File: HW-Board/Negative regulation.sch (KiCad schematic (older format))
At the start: 26 parts, among them Q3 BCX56, U10 AD5245, U11 OP07, U12 OP07, U13 OP07, U14 INA219POS, U15 OP07, U9 MCP4725

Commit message: sync
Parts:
- added Rin1: 100K 1%, symbol Device:R
- renumbered Rin1 to Rf1, Rf1 to Rf2, R11 to Rf3, R10 to Rin3
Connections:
- net at Rf1.1, U11.2 (-): now also Rin1.2; no longer U10.7 (B)
- new net: Rin1.1, U10.7 (B)
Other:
- note added: "Flip to negative"
- note added: "Flip to positive"
- note added: "LM395?"
- note removed: "Todo:\n\nMerge to fewer opamps"
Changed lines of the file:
@@
 	8050 2900 8000 2900
 $Comp
-L Device:R R10
+L Device:R Rin3
 U 1 1 5D005FD1
 P 8250 2650
-F 0 "R10" V 8043 2650 50  0000 C CNN
+F 0 "Rin3" V 8043 2650 50  0000 C CNN
 F 1 "100K 1%" V 8134 2650 50  0000 C CNN
 F 2 "" V 8180 2650 50  0001 C CNN
@@
 	8250 2950 8250 2850
 $Comp
-L Device:R R11
+L Device:R Rf3
 U 1 1 5D005FD8
 P 8800 3150
-F 0 "R11" V 8593 3150 50  0000 C CNN
+F 0 "Rf3" V 8593 3150 50  0000 C CNN
 F 1 "100K 1%" V 8684 3150 50  0000 C CNN
 F 2 "" V 8730 3150 50  0001 C CNN
@@
 	6950 3000 6950 2900
 $Comp
-L Device:R Rf1
+L Device:R Rf2
 U 1 1 5D006004
 P 7500 3200
-F 0 "Rf1" V 7293 3200 50  0000 C CNN
+F 0 "Rf2" V 7293 3200 50  0000 C CNN
 F 1 "100K 1%" V 7384 3200 50  0000 C CNN
 F 2 "" V 7430 3200 50  0001 C CNN
@@
 Connection ~ 8250 2200
 Connection ~ 6950 2200
-Text Notes 5750 3800 0    50   ~ 0
+Text Notes 3450 950  0    50   ~ 0
 Inverting AMP:\nVout=  -Rf/Rin x Vin
 $Comp
@@
 $EndComp
 $Comp
-L Device:R Rin1
+L Device:R Rf1
 U 1 1 5CFD1CAF
 P 4050 3850
-F 0 "Rin1" V 3843 3850 50  0000 C CNN
+F 0 "Rf1" V 3843 3850 50  0000 C CNN
 F 1 "100K 1%" V 3934 3850 50  0000 C CNN
 F 2 "" V 3980 3850 50  0001 C CNN
@@
 $EndComp
 Wire Wire Line
-	3250 3300 3750 3300
+	3250 3300 3350 3300
 $Comp
 L power:GNDA #PWR0210
@@
 Wire Wire Line
 	3400 3550 3500 3550
-Text Notes 3000 5650 0    50   ~ 0
-Todo:\n\nMerge to fewer opamps
+Text Notes 3900 4200 0    50   ~ 0
+Flip to negative
+$Comp
+L Device:R Rin1
+U 1 1 5CF6E0E8
+P 3500 3300
+F 0 "Rin1" V 3293 3300 50  0000 C CNN
+F 1 "100K 1%" V 3384 3300 50  0000 C CNN
+F 2 "" V 3430 3300 50  0001 C CNN
+F 3 "~" H 3500 3300 50  0001 C CNN
+	1    3500 3300
+	0    -1   -1   0
+$EndComp
+Wire Wire Line
+	3650 3300 3750 3300
+Text Notes 6450 3950 0    50   ~ 0
+Flip to positive
+Wire Notes Line
+	6300 2450 6300 4000
+Wire Notes Line
+	6300 4000 8900 4000
+Wire Notes Line
+	8900 4000 8900 2450
+Wire Notes Line
+	8900 2450 6300 2450
+Wire Notes Line
+	3400 4450 4500 4450
+Wire Notes Line
+	4500 4450 4500 1950
+Wire Notes Line
+	4500 1950 3400 1950
+Wire Notes Line
+	3400 1950 3400 4450
+Text Notes 5800 1850 0    50   ~ 0
+LM395?
 $EndSCHEMATC

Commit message: sync
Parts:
- added C?: 10u, symbol Device:C_Small
- added C?: 100n, symbol Device:C_Small
- added JP?: Jumper, symbol Device:Jumper
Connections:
- net +3V3: now also C?.1, C?.1
- net GNDA: now also C?.2, C?.2
- net at Rin1.1: now also U10.1 (W), JP?.2; no longer U10.7 (B)
- net at U9.1 (VoutA): now also U10.7 (B), JP?.1; no longer U10.1 (W)
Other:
- moved on the sheet: C26, C27, Rin1, U10, U9

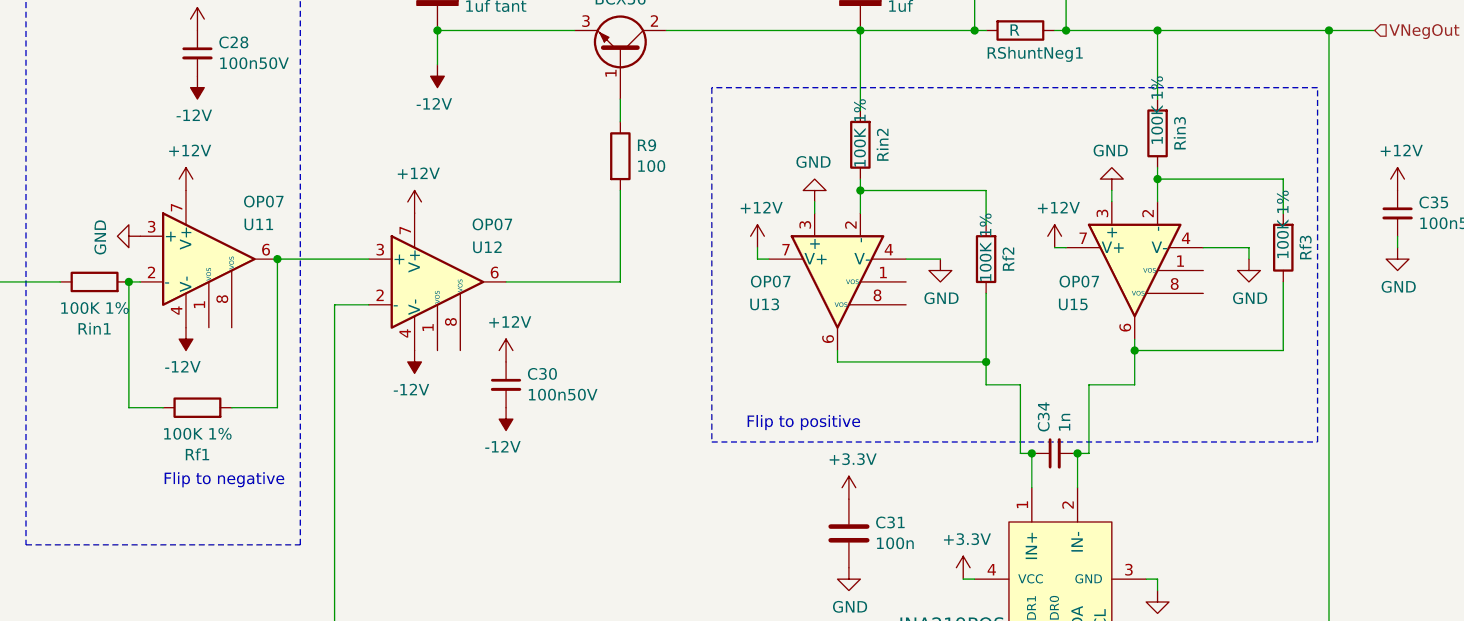
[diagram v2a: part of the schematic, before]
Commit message: Changed OPAMP on negative rail
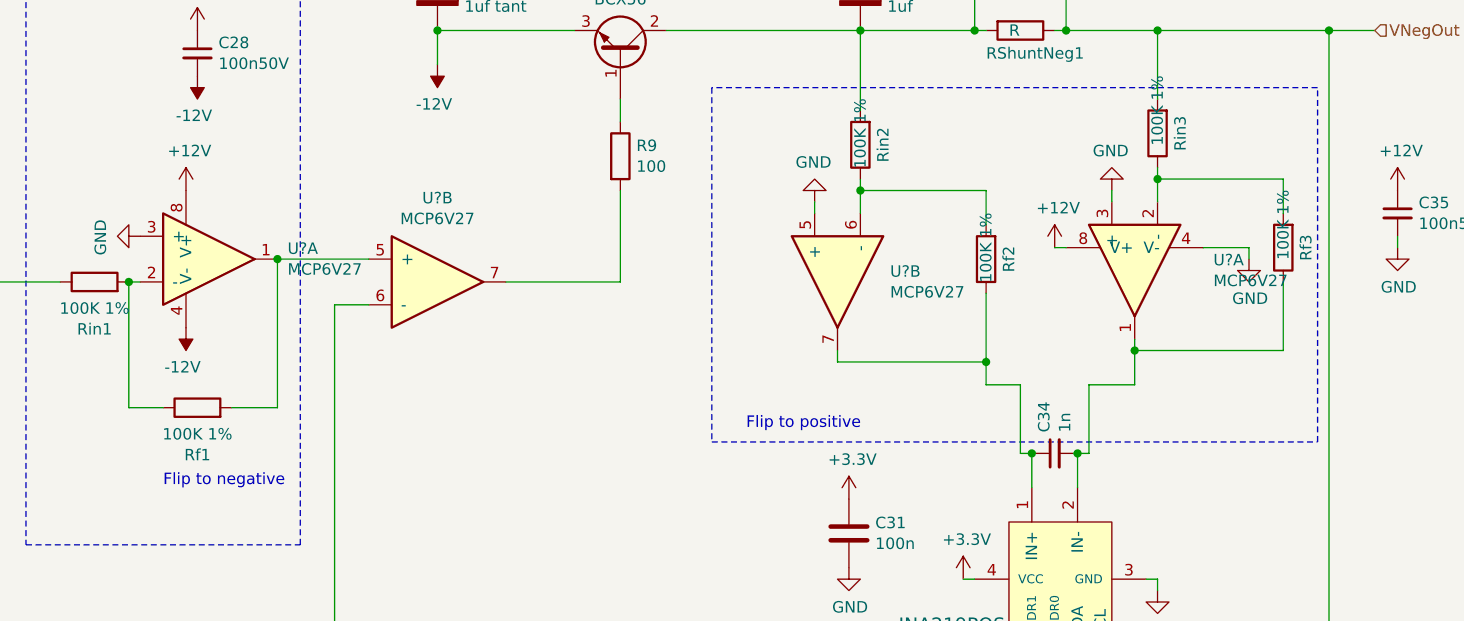
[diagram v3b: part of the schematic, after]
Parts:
- removed C30: 100n50V, symbol Device:C_Small
- removed U11, U12, U13, U15: OP07, symbol Amplifier_Operational:OP07
- added U? (x4): MCP6V27, Package_SO:SOIC-8_3.9x4.9mm_P1.27mm, symbol Peters:MCP6V27
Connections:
- net +12V: now also U?.8 (V+), U?.8 (V+)
- net -12V: now also U?.4 (V-)
- net GND: now also U?.3 (+), U?.3 (+), U?.4 (V-), U?.5 (+)
- net VNegOut: now also U?.6 (-)
- net at Rf1.1, Rin1.2: now also U?.2 (-)
- net at Rf1.2: now also U?.1, U?.5 (+)
- net at R9.2: now also U?.7
- net at Rf3.2, Rin3.1: now also U?.2 (-)
- net at C34.2, Rf3.1, U14.2 (IN-): now also U?.1
- net at Rf2.2, Rin2.1: now also U?.6 (-)
- net at C34.1, Rf2.1, U14.1 (IN+): now also U?.7
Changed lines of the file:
@@
 	8650 3150 8450 3150
-$Comp
-L power:+12V #PWR0177
-U 1 1 5D005FE8
-P 6500 3150
-F 0 "#PWR0177" H 6500 3000 50  0001 C CNN
-F 1 "+12V" H 6515 3323 50  0000 C CNN
-F 2 "" H 6500 3150 50  0001 C CNN
-F 3 "" H 6500 3150 50  0001 C CNN
-	1    6500 3150
-	1    0    0    -1
-$EndComp
-Wire Wire Line
-	6550 3200 6500 3200
 $Comp
 L power:GND #PWR0178
@@
 Text Notes 3450 950  0    50   ~ 0
 Inverting AMP:\nVout=  -Rf/Rin x Vin
-$Comp
-L Amplifier_Operational:OP07 U13
-U 1 1 5D006074
-P 6850 3300
-F 0 "U13" V 6950 3550 50  0000 L CNN
-F 1 "OP07" V 6850 3500 50  0000 L CNN
-F 2 "" H 6900 3350 50  0001 C CNN
-F 3 "https://www.analog.com/media/en/technical-documentation/data-sheets/OP07.pdf" H 6900 3450 50  0001 C CNN
-	1    6850 3300
-	0    -1   1    0
-$EndComp
-$Comp
-L Amplifier_Operational:OP07 U15
-U 1 1 5D00607A
-P 8150 3250
-F 0 "U15" V 8300 3450 50  0000 L CNN
-F 1 "OP07" V 8200 3400 50  0000 L CNN
-F 2 "" H 8200 3300 50  0001 C CNN
-F 3 "https://www.analog.com/media/en/technical-documentation/data-sheets/OP07.pdf" H 8200 3400 50  0001 C CNN
-	1    8150 3250
-	0    -1   1    0
-$EndComp
 Text HLabel 7900 5050 3    50   Input ~ 0
 I2C_SDA
@@
 	5100 1900 5100 1850
 $Comp
-L Amplifier_Operational:OP07 U11
-U 1 1 5CFD0F5A
-P 4100 3200
-F 0 "U11" H 4250 3350 50  0000 L CNN
-F 1 "OP07" H 4250 3450 50  0000 L CNN
-F 2 "" H 4150 3250 50  0001 C CNN
-F 3 "https://www.analog.com/media/en/technical-documentation/data-sheets/OP07.pdf" H 4150 3350 50  0001 C CNN
-	1    4100 3200
-	1    0    0    -1
-$EndComp
-$Comp
 L Device:R Rf1
 U 1 1 5CFD1CAF
@@
 	0    1    -1   0
 $EndComp
-$Comp
-L Amplifier_Operational:OP07 U12
-U 1 1 5CFF7597
-P 5100 3300
-F 0 "U12" H 5250 3450 50  0000 L CNN
-F 1 "OP07" H 5250 3550 50  0000 L CNN
-F 2 "" H 5150 3350 50  0001 C CNN
-F 3 "https://www.analog.com/media/en/technical-documentation/data-sheets/OP07.pdf" H 5150 3450 50  0001 C CNN
-	1    5100 3300
-	1    0    0    -1
-$EndComp
 Wire Wire Line
 	5400 3300 5900 3300
@@
 $EndComp
 $Comp
-L Device:C_Small C30
-U 1 1 5D0227CE
-P 5400 3750
-F 0 "C30" H 5492 3796 50  0000 L CNN
-F 1 "100n50V" H 5492 3705 50  0000 L CNN
-F 2 "" H 5400 3750 50  0001 C CNN
-F 3 "~" H 5400 3750 50  0001 C CNN
-	1    5400 3750
-	1    0    0    -1
-$EndComp
-$Comp
-L power:+12V #PWR0199
-U 1 1 5D0227D8
-P 5400 3650
-F 0 "#PWR0199" H 5400 3500 50  0001 C CNN
-F 1 "+12V" H 5415 3823 50  0000 C CNN
-F 2 "" H 5400 3650 50  0001 C CNN
-F 3 "" H 5400 3650 50  0001 C CNN
-	1    5400 3650
-	1    0    0    -1
-$EndComp
-$Comp
-L power:-12V #PWR0200
-U 1 1 5D0227E2
-P 5400 3850
-F 0 "#PWR0200" H 5400 3950 50  0001 C CNN
-F 1 "-12V" H 5415 4023 50  0000 C CNN
-F 2 "" H 5400 3850 50  0001 C CNN
-F 3 "" H 5400 3850 50  0001 C CNN
-	1    5400 3850
-	-1   0    0    1
-$EndComp
-$Comp
 L Device:C_Small C35
 U 1 1 5D027EE0
@@
 $EndComp
 $Comp
-L power:GND #PWR0203
-U 1 1 5D005FEE
-P 7300 3200
-F 0 "#PWR0203" H 7300 2950 50  0001 C CNN
-F 1 "GND" H 7305 3027 50  0000 C CNN
-F 2 "" H 7300 3200 50  0001 C CNN
-F 3 "" H 7300 3200 50  0001 C CNN
-	1    7300 3200
-	1    0    0    -1
-$EndComp
-$Comp
 L power:GND #PWR0204
 U 1 1 5D005FC2
@@
 Wire Wire Line
 	9850 3200 9850 3150
-$Comp
-L power:-12V #PWR0207
-U 1 1 5D03DC23
-P 5000 3600
-F 0 "#PWR0207" H 5000 3700 50  0001 C CNN
-F 1 "-12V" H 5015 3773 50  0000 C CNN
-F 2 "" H 5000 3600 50  0001 C CNN
-F 3 "" H 5000 3600 50  0001 C CNN
-	1    5000 3600
-	-1   0    0    1
-$EndComp
-$Comp
-L power:+12V #PWR0208
-U 1 1 5D03E477
-P 5000 3000
-F 0 "#PWR0208" H 5000 2850 50  0001 C CNN
-F 1 "+12V" H 5015 3173 50  0000 C CNN
-F 2 "" H 5000 3000 50  0001 C CNN
-F 3 "" H 5000 3000 50  0001 C CNN
-	1    5000 3000
-	1    0    0    -1
-$EndComp
 Wire Wire Line
 	6100 2200 6950 2200
 Wire Wire Line
 	4800 3200 4400 3200
-Connection ~ 4400 3200
 Wire Wire Line
 	4800 3400 4650 3400
@@
 Wire Wire Line
 	2850 3300 3450 3300
-Wire Wire Line
-	6500 3200 6500 3150
-Wire Wire Line
-	7300 3200 7150 3200
+$Comp
+L Peters:MCP6V27 U?
+U 1 1 5D46FBA9
+P 8150 3250
+F 0 "U?" V 8104 2906 50  0000 R CNN
+F 1 "MCP6V27" V 8195 2906 50  0000 R CNN
+F 2 "Package_SO:SOIC-8_3.9x4.9mm_P1.27mm" H 8050 3950 50  0001 C CNN
+F 3 "http://ww1.microchip.com/downloads/en/devicedoc/25007b.pdf" H 8150 3250 50  0001 C CNN
+	1    8150 3250
+	0    -1   1    0
+$EndComp
+$Comp
+L Peters:MCP6V27 U?
+U 2 1 5D473C75
+P 6850 3300
+F 0 "U?" V 6804 3070 50  0000 R CNN
+F 1 "MCP6V27" V 6895 3070 50  0000 R CNN
+F 2 "Package_SO:SOIC-8_3.9x4.9mm_P1.27mm" H 6750 4000 50  0001 C CNN
+F 3 "http://ww1.microchip.com/downloads/en/devicedoc/25007b.pdf" H 6850 3300 50  0001 C CNN
+	2    6850 3300
+	0    -1   1    0
+$EndComp
+$Comp
+L Peters:MCP6V27 U?
+U 2 1 5D4831BF
+P 5100 3300
+F 0 "U?" H 5100 3667 50  0000 C CNN
+F 1 "MCP6V27" H 5100 3576 50  0000 C CNN
+F 2 "Package_SO:SOIC-8_3.9x4.9mm_P1.27mm" H 5000 4000 50  0001 C CNN
+F 3 "http://ww1.microchip.com/downloads/en/devicedoc/25007b.pdf" H 5100 3300 50  0001 C CNN
+	2    5100 3300
+	1    0    0    -1
+$EndComp
+$Comp
+L Peters:MCP6V27 U?
+U 1 1 5D48E79E
+P 4100 3200
+F 0 "U?" H 4444 3246 50  0000 L CNN
+F 1 "MCP6V27" H 4444 3155 50  0000 L CNN
+F 2 "Package_SO:SOIC-8_3.9x4.9mm_P1.27mm" H 4000 3900 50  0001 C CNN
+F 3 "http://ww1.microchip.com/downloads/en/devicedoc/25007b.pdf" H 4100 3200 50  0001 C CNN
+	1    4100 3200
+	1    0    0    -1
+$EndComp
+Connection ~ 4400 3200
 $EndSCHEMATC

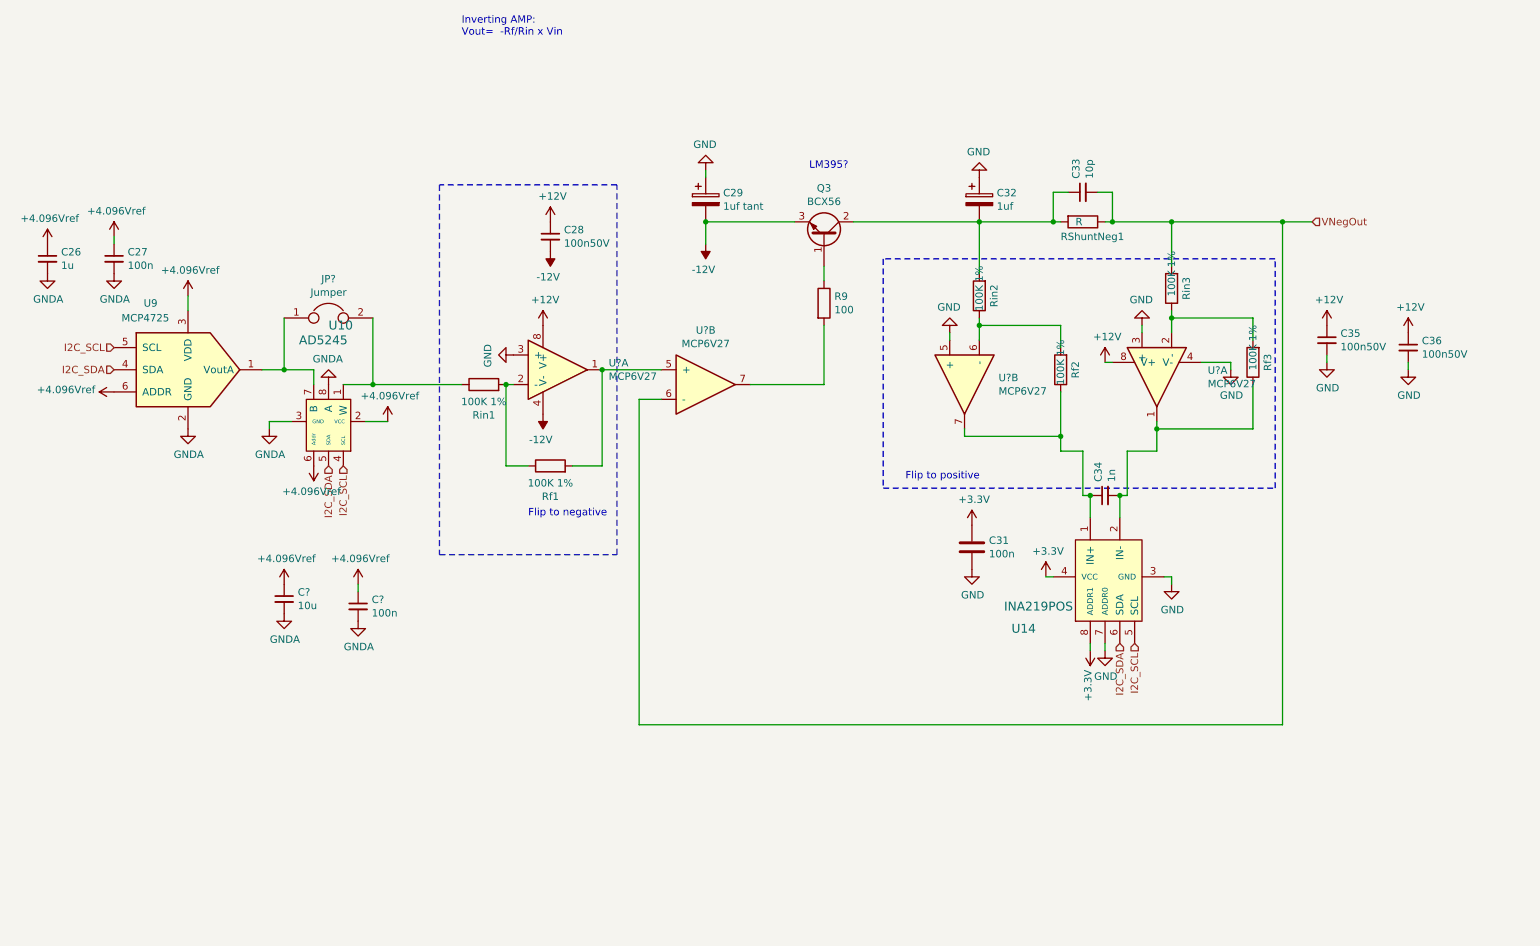
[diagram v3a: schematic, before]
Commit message: 5v isolation and better opamps
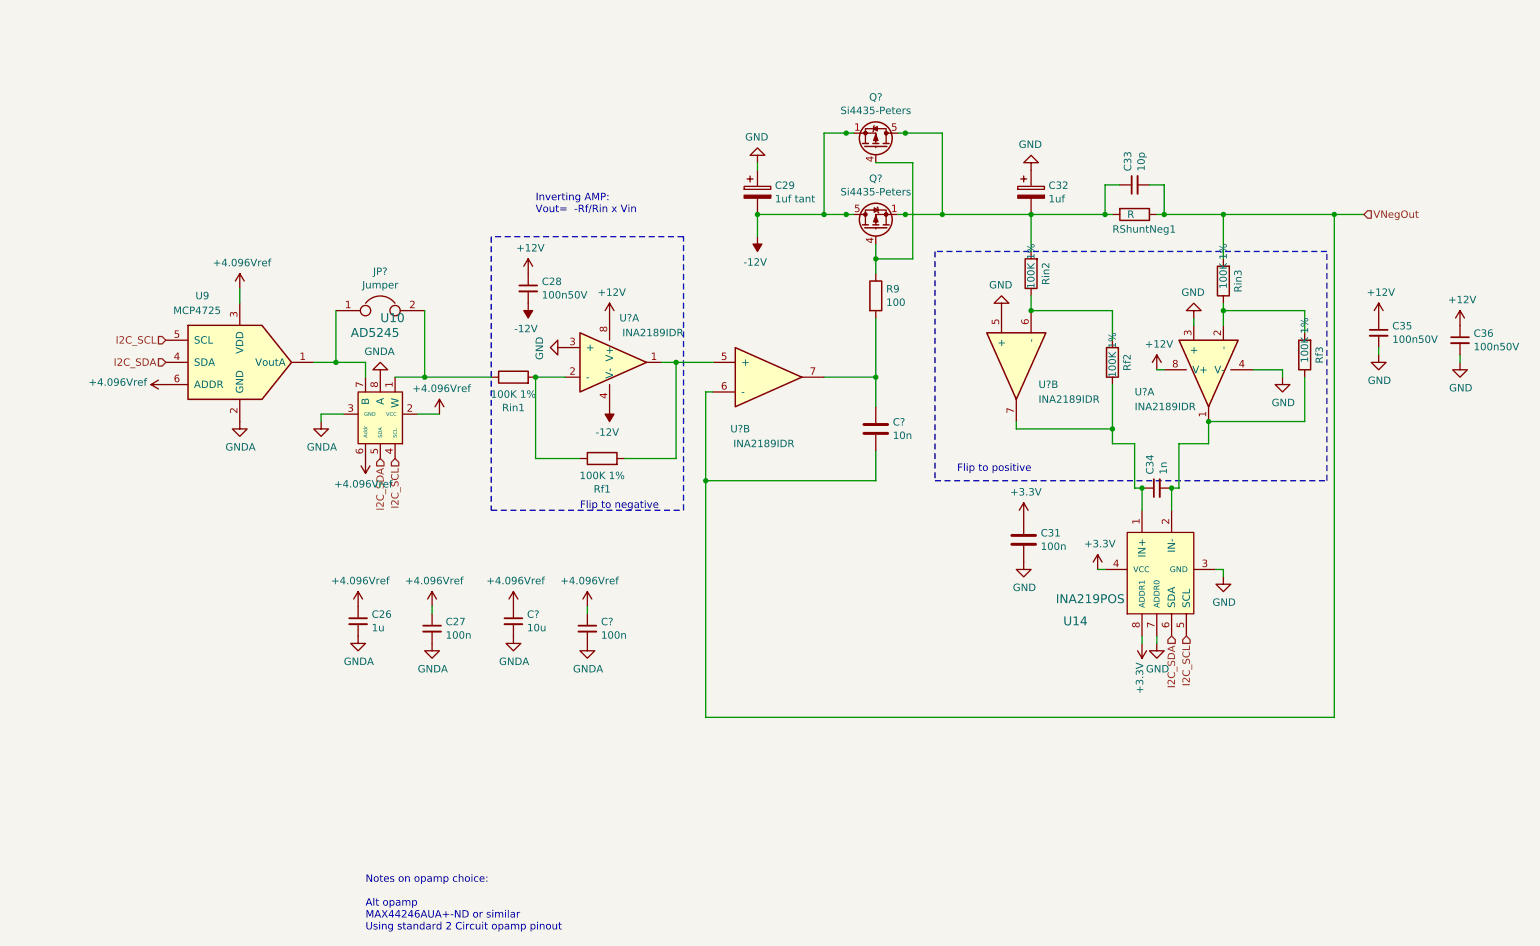
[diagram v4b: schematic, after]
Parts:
- removed Q3: BCX56, Package_TO_SOT_SMD:SOT-89-3, symbol Transistor_BJT:BCX56
- removed U? (x4): MCP6V27, Package_SO:SOIC-8_3.9x4.9mm_P1.27mm, symbol Peters:MCP6V27
- added C?: 10n, symbol Device:C
- added Q? (x2): Si4435-Peters, Package_SO:SOIC-8_3.9x4.9mm_P1.27mm, symbol BreadbaordPSU-rescue:Si4435-Peters
- added U? (x4): INA2189IDR, Package_SO:SO-8_3.9x4.9mm_P1.27mm, symbol Peters:INA2189IDR
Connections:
- net +12V: now also U?.8 (V+), U?.8 (V+)
- net -12V: now also Q?.1 (S), Q?.2 (S), Q?.3 (S), Q?.5 (D), Q?.6 (D), Q?.7 (D), Q?.8 (D), U?.4 (V-)
- net GND: now also U?.3 (+), U?.3 (+), U?.4 (V-), U?.5 (+)
- net VNegOut: now also C?.2, U?.6 (-)
- net at Rf1.1, Rin1.2: now also U?.2 (-)
- net at Rf1.2: now also U?.1, U?.5 (+)
- net at R9.1: now also Q?.4 (G), Q?.4 (G)
- net at C32.2, C33.1, RShuntNeg1.2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: now also Q?.1 (S), Q?.2 (S), Q?.3 (S), Q?.5 (D), Q?.6 (D), Q?.7 (D), Q?.8 (D)
- net at R9.2: now also C?.1, U?.7
- net at Rf3.2, Rin3.1: now also U?.2 (-)
- net at C34.2, Rf3.1, U14.2 (IN-): now also U?.1
- net at Rf2.2, Rin2.1: now also U?.6 (-)
- net at C34.1, Rf2.1, U14.1 (IN+): now also U?.7
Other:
- note added: "Notes on opamp choice:\n\nAlt opamp\nMAX44246AUA+-ND or similar\nUsing standard 2 Circuit opamp pinout"
- note removed: "LM395?"
- moved on the sheet: C26, C27, C28, C29, C31, C32, C33, C34, C35, C36, C?, JP?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
